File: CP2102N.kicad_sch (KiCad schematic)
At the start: 19 parts, among them J1 USB4110GFA, U9 CP2102N-A02-GQFN24R

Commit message: backups removalled schematic looking correct if not good
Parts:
- removed C15: 100nF, robot-cortex:C_0402_1005Metric, symbol robot-cortex:Capacitor
- removed D8: ESD9B3.3ST5G, robot-cortex:D_SOD-923, symbol robot-cortex:ESD9B3.3ST5G
- removed R4: 10k, robot-cortex:R_0402_1005Metric, symbol robot-cortex:Resistor
- added D4, D5: 150060GS84000, robot-cortex:LED_0603_1608Metric, symbol foc-pcb:LED
- added R2, R3: 470, robot-cortex:R_0402_1005Metric, symbol foc-pcb:Resistor
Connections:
- net 3V3: now also R2.1, R3.1; no longer C20.1, C21.1, U9.7 (VREGIN)
- net CP2102_RX: now also D4.1 (K)
- net CP2102_TX: now also D5.1 (K)
- net VUSB: now also C20.1, C21.1, U9.7 (VREGIN)
- net RS485: now reaches U9.12 (GPIO.2/RS485)
- net RTS: no longer names the net of U9.19 (~{RTS})
- new net: D4.2 (A), R2.2
- new net: D5.2 (A), R3.2
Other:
- note removed: "Tying VDD and VREGIN is for when the regulator is not used."
- moved on the sheet: C20, C21

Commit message: library table
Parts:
- C16, C17, C18, C19, C20, C21, C4: symbol robot-cortex:Capacitor -> usb-rs485:Capacitor
- D1, D2, D3: symbol robot-cortex:ESD9B3.3ST5G -> usb-rs485:ESD9B3.3ST5G
- D4, D5: symbol foc-pcb:LED -> usb-rs485:LED
- J1: symbol robot-cortex:USB4110GFA -> usb-rs485:USB4110GFA
- R1: symbol NeuralStimulatorAndRecorder:Resistor -> usb-rs485:Resistor
- R2, R3: symbol foc-pcb:Resistor -> usb-rs485:Resistor
- R7, R8, R9: symbol robot-cortex:Resistor -> usb-rs485:Resistor
- U9: symbol robot-cortex:CP2102N-A02-GQFN24R -> usb-rs485:CP2102N-A02-GQFN24R
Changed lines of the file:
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@@
     )
   )
-  (symbol (lib_id "robot-cortex:Resistor") (at 253.365 34.29 0) (mirror x) (unit 1)
+  (symbol (lib_id "usb-rs485:Resistor") (at 253.365 34.29 0) (mirror x) (unit 1)
     (in_bom yes) (on_board yes) (dnp no)
     (property "Reference" "R7" (at 250.825 33.655 0)
@@
     )
   )
-  (symbol (lib_id "robot-cortex:ESD9B3.3ST5G") (at 82.55 133.985 90) (unit 1)
+  (symbol (lib_id "usb-rs485:ESD9B3.3ST5G") (at 82.55 133.985 90) (unit 1)
     (in_bom yes) (on_board yes) (dnp no)
     (property "Reference" "D1" (at 78.74 133.985 90)
@@
     )
   )
-  (symbol (lib_id "robot-cortex:ESD9B3.3ST5G") (at 87.63 133.985 90) (unit 1)
+  (symbol (lib_id "usb-rs485:ESD9B3.3ST5G") (at 87.63 133.985 90) (unit 1)
     (in_bom yes) (on_board yes) (dnp no)
     (property "Reference" "D2" (at 85.09 133.985 90)
@@
     )
   )
-  (symbol (lib_id "robot-cortex:USB4110GFA") (at 112.395 108.585 0) (unit 1)
+  (symbol (lib_id "usb-rs485:USB4110GFA") (at 112.395 108.585 0) (unit 1)
     (in_bom yes) (on_board yes) (dnp no) (fields_autoplaced)
     (property "Reference" "J1" (at 112.395 93.345 0)
@@
     )
   )
-  (symbol (lib_id "robot-cortex:Capacitor") (at 186.69 102.87 0) (unit 1)
+  (symbol (lib_id "usb-rs485:Capacitor") (at 186.69 102.87 0) (unit 1)
     (in_bom yes) (on_board yes) (dnp no) (fields_autoplaced)
     (property "Reference" "C20" (at 189.865 102.235 0)
@@
     )
   )
-  (symbol (lib_id "robot-cortex:Capacitor") (at 198.12 102.87 0) (unit 1)
+  (symbol (lib_id "usb-rs485:Capacitor") (at 198.12 102.87 0) (unit 1)
     (in_bom yes) (on_board yes) (dnp no)
     (property "Reference" "C21" (at 200.66 102.235 0)
@@
     )
   )
-  (symbol (lib_id "robot-cortex:Capacitor") (at 57.15 36.195 0) (unit 1)
+  (symbol (lib_id "usb-rs485:Capacitor") (at 57.15 36.195 0) (unit 1)
     (in_bom yes) (on_board yes) (dnp no) (fields_autoplaced)
     (property "Reference" "C17" (at 60.325 35.56 0)
@@
     )
   )
-  (symbol (lib_id "robot-cortex:Capacitor") (at 69.85 36.83 0) (unit 1)
+  (symbol (lib_id "usb-rs485:Capacitor") (at 69.85 36.83 0) (unit 1)
     (in_bom yes) (on_board yes) (dnp no) (fields_autoplaced)
     (property "Reference" "C18" (at 73.025 36.195 0)
@@
     )
   )
-  (symbol (lib_id "foc-pcb:LED") (at 160.02 126.365 90) (unit 1)
+  (symbol (lib_id "usb-rs485:LED") (at 160.02 126.365 90) (unit 1)
     (in_bom yes) (on_board yes) (dnp no)
     (property "Reference" "D4" (at 155.575 126.365 90)
@@
     )
   )
-  (symbol (lib_id "robot-cortex:Resistor") (at 264.795 112.395 0) (mirror x) (unit 1)
+  (symbol (lib_id "usb-rs485:Resistor") (at 264.795 112.395 0) (mirror x) (unit 1)
     (in_bom yes) (on_board yes) (dnp no)
     (property "Reference" "R9" (at 262.89 109.855 90)
@@
     )
   )
-  (symbol (lib_id "robot-cortex:CP2102N-A02-GQFN24R") (at 234.315 128.905 0) (unit 1)
+  (symbol (lib_id "usb-rs485:CP2102N-A02-GQFN24R") (at 234.315 128.905 0) (unit 1)
     (in_bom yes) (on_board yes) (dnp no) (fields_autoplaced)
     (property "Reference" "U9" (at 234.315 100.965 0)
@@
     )
   )
-  (symbol (lib_id "robot-cortex:Capacitor") (at 44.45 36.195 0) (unit 1)
+  (symbol (lib_id "usb-rs485:Capacitor") (at 44.45 36.195 0) (unit 1)
     (in_bom yes) (on_board yes) (dnp no) (fields_autoplaced)
     (property "Reference" "C16" (at 47.625 35.56 0)
@@
     )
   )
-  (symbol (lib_id "foc-pcb:Resistor") (at 160.02 116.205 0) (unit 1)
+  (symbol (lib_id "usb-rs485:Resistor") (at 160.02 116.205 0) (unit 1)
     (in_bom yes) (on_board yes) (dnp no) (fields_autoplaced)
     (property "Reference" "R2" (at 162.56 116.84 0)
@@
     )
   )
-  (symbol (lib_id "robot-cortex:Resistor") (at 253.365 44.45 0) (mirror x) (unit 1)
+  (symbol (lib_id "usb-rs485:Resistor") (at 253.365 44.45 0) (mirror x) (unit 1)
     (in_bom yes) (on_board yes) (dnp no)
     (property "Reference" "R8" (at 250.4766 43.815 0)
@@
     )
   )
-  (symbol (lib_id "foc-pcb:Resistor") (at 166.37 116.205 0) (unit 1)
+  (symbol (lib_id "usb-rs485:Resistor") (at 166.37 116.205 0) (unit 1)
     (in_bom yes) (on_board yes) (dnp no) (fields_autoplaced)
     (property "Reference" "R3" (at 168.91 116.84 0)
@@
     )
   )
-  (symbol (lib_id "robot-cortex:Capacitor") (at 137.795 99.695 0) (unit 1)
+  (symbol (lib_id "usb-rs485:Capacitor") (at 137.795 99.695 0) (unit 1)
     (in_bom yes) (on_board yes) (dnp no) (fields_autoplaced)
     (property "Reference" "C4" (at 140.97 99.06 0)
@@
     )
   )
-  (symbol (lib_id "foc-pcb:LED") (at 166.37 126.365 90) (unit 1)
+  (symbol (lib_id "usb-rs485:LED") (at 166.37 126.365 90) (unit 1)
     (in_bom yes) (on_board yes) (dnp no)
     (property "Reference" "D5" (at 169.545 126.365 90)
@@
     )
   )
-  (symbol (lib_id "robot-cortex:ESD9B3.3ST5G") (at 92.71 133.985 90) (unit 1)
+  (symbol (lib_id "usb-rs485:ESD9B3.3ST5G") (at 92.71 133.985 90) (unit 1)
     (in_bom yes) (on_board yes) (dnp no)
     (property "Reference" "D3" (at 90.17 133.985 90)
@@
     )
   )
-  (symbol (lib_id "NeuralStimulatorAndRecorder:Resistor") (at 88.265 102.235 90) (unit 1)
+  (symbol (lib_id "usb-rs485:Resistor") (at 88.265 102.235 90) (unit 1)
     (in_bom yes) (on_board yes) (dnp no)
     (property "Reference" "R1" (at 90.805 99.695 90)
@@
     )
   )
-  (symbol (lib_id "robot-cortex:Capacitor") (at 81.28 36.83 0) (unit 1)
+  (symbol (lib_id "usb-rs485:Capacitor") (at 81.28 36.83 0) (unit 1)
     (in_bom yes) (on_board yes) (dnp no)
     (property "Reference" "C19" (at 83.82 36.195 0)

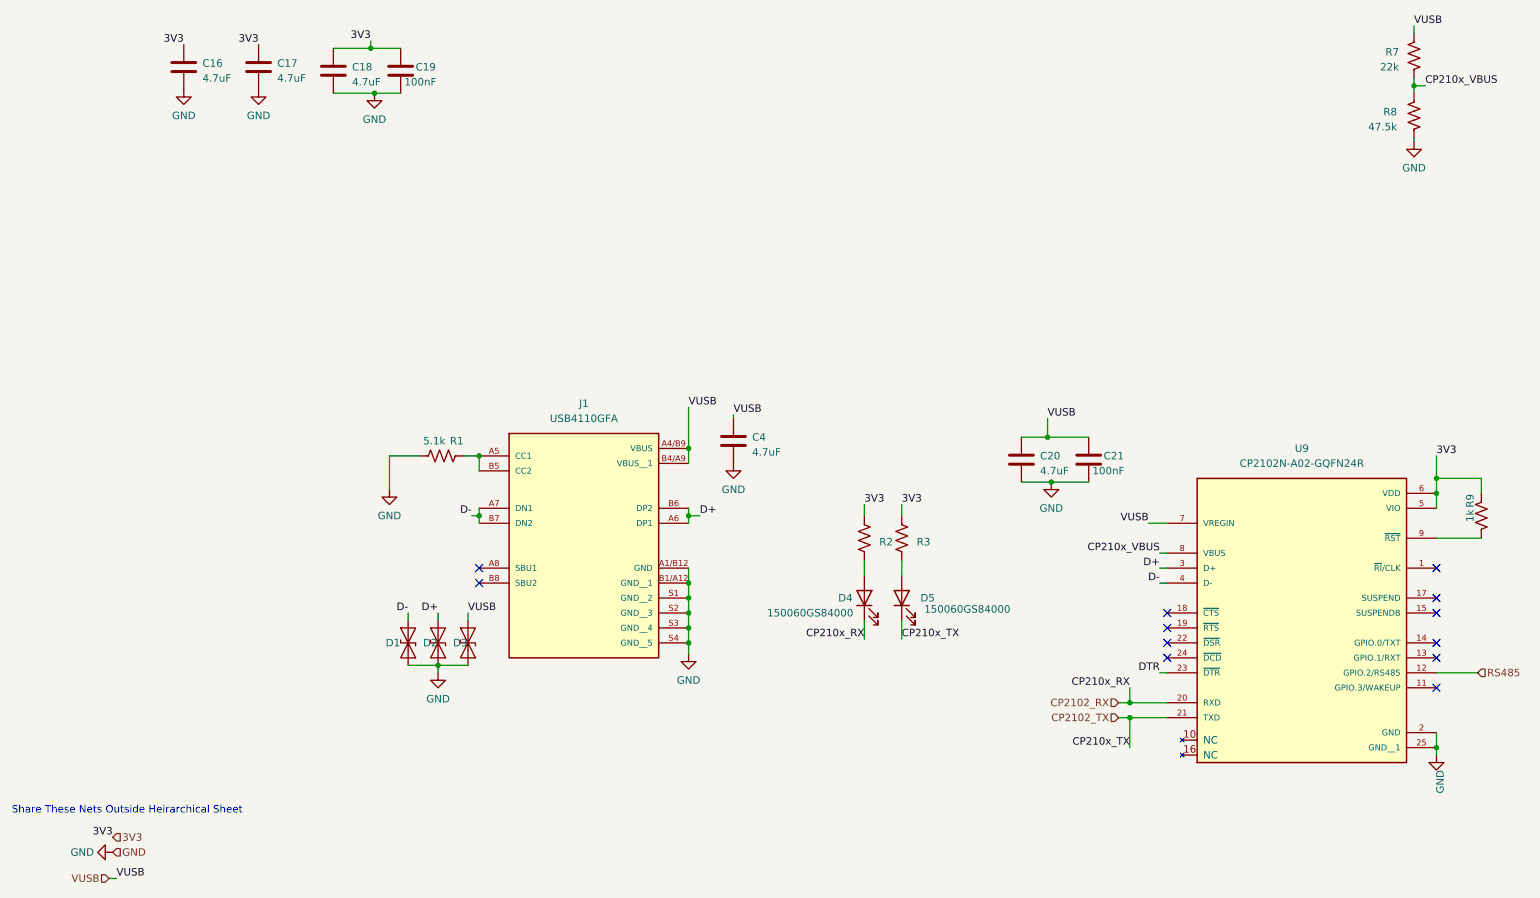
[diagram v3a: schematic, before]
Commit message: cleanup some routing
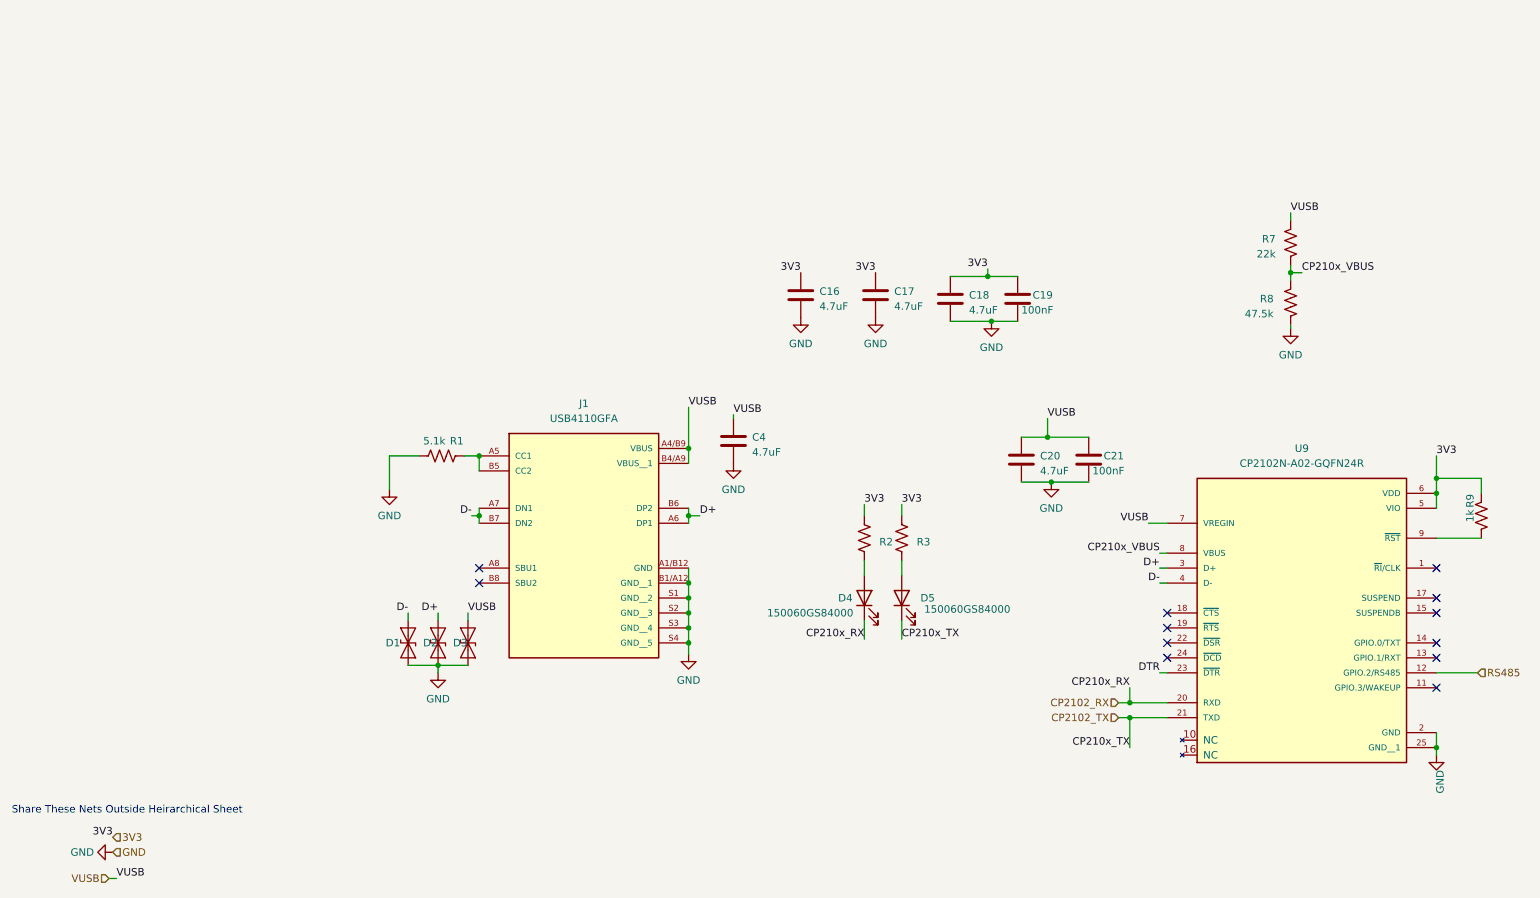
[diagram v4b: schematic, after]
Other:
- moved on the sheet: C16, C17, C18, C19, R7, R8

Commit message: routing
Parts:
- removed C16, C17, C18: 4.7uF, robot-cortex:C_0603_1608Metric, symbol usb-rs485:Capacitor
- removed C19: 100nF, robot-cortex:C_0402_1005Metric, symbol usb-rs485:Capacitor
- added C5: 4.7uF 0603, robot-cortex:C_0603_1608Metric, symbol usb-rs485:Capacitor
- added C8: 100nF, robot-cortex:C_0402_1005Metric, symbol usb-rs485:Capacitor
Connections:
- net GND: now also C5.2, C8.2
- new net +3V3: C5.1, C8.1

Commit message: rename library to be for this
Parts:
- C20, C4, C5: footprint robot-cortex:C_0603_1608Metric -> usb-rs485:C_0603_1608Metric
- C21, C8: footprint robot-cortex:C_0402_1005Metric -> usb-rs485:C_0402_1005Metric
- D1, D2, D3: footprint robot-cortex:D_SOD-923 -> usb-rs485:D_SOD-923
- D4, D5: footprint robot-cortex:LED_0603_1608Metric -> usb-rs485:LED_0603_1608Metric
- J1: footprint robot-cortex:GCT_USB4110GFA -> usb-rs485:GCT_USB4110GFA
- R1, R2, R3, R7, R8, R9: footprint robot-cortex:R_0402_1005Metric -> usb-rs485:R_0402_1005Metric
- U9: footprint robot-cortex:QFN50P400X400X80-25N -> usb-rs485:QFN50P400X400X80-25N
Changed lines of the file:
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@@
       (effects (font (size 1.27 1.27)) (justify right))
     )
-    (property "Footprint" "robot-cortex:R_0402_1005Metric" (at 227.33 78.74 0)
+    (property "Footprint" "usb-rs485:R_0402_1005Metric" (at 227.33 78.74 0)
       (effects (font (size 1.27 1.27)) hide)
     )
@@
       (effects (font (size 1.27 1.27)) (justify right) hide)
     )
-    (property "Footprint" "robot-cortex:D_SOD-923" (at 77.47 131.445 0)
+    (property "Footprint" "usb-rs485:D_SOD-923" (at 77.47 131.445 0)
       (effects (font (size 1.27 1.27)) hide)
     )
@@
       (effects (font (size 1.27 1.27)) (justify right) hide)
     )
-    (property "Footprint" "robot-cortex:D_SOD-923" (at 82.55 131.445 0)
+    (property "Footprint" "usb-rs485:D_SOD-923" (at 82.55 131.445 0)
       (effects (font (size 1.27 1.27)) hide)
     )
@@
       (effects (font (size 1.27 1.27)))
     )
-    (property "Footprint" "robot-cortex:GCT_USB4110GFA" (at 112.395 108.585 0)
+    (property "Footprint" "usb-rs485:GCT_USB4110GFA" (at 112.395 108.585 0)
       (effects (font (size 1.27 1.27)) (justify bottom) hide)
     )
@@
       (effects (font (size 1.27 1.27)) (justify left))
     )
-    (property "Footprint" "robot-cortex:C_0603_1608Metric" (at 187.6552 106.68 0)
+    (property "Footprint" "usb-rs485:C_0603_1608Metric" (at 187.6552 106.68 0)
       (effects (font (size 1.27 1.27)) hide)
     )
@@
       (effects (font (size 1.27 1.27)) (justify left))
     )
-    (property "Footprint" "robot-cortex:C_0402_1005Metric" (at 199.0852 106.68 0)
+    (property "Footprint" "usb-rs485:C_0402_1005Metric" (at 199.0852 106.68 0)
       (effects (font (size 1.27 1.27)) hide)
     )
@@
       (effects (font (size 1.27 1.27)) (justify left))
     )
-    (property "Footprint" "robot-cortex:C_0402_1005Metric" (at 115.9002 82.55 0)
+    (property "Footprint" "usb-rs485:C_0402_1005Metric" (at 115.9002 82.55 0)
       (effects (font (size 1.27 1.27)) hide)
     )
@@
       (effects (font (size 1.27 1.27)) (justify left))
     )
-    (property "Footprint" "robot-cortex:C_0603_1608Metric" (at 107.6198 82.55 0)
+    (property "Footprint" "usb-rs485:C_0603_1608Metric" (at 107.6198 82.55 0)
       (effects (font (size 1.27 1.27)) hide)
     )
@@
       (effects (font (size 1.27 1.27)) (justify right))
     )
-    (property "Footprint" "robot-cortex:LED_0603_1608Metric" (at 160.02 126.365 0)
+    (property "Footprint" "usb-rs485:LED_0603_1608Metric" (at 160.02 126.365 0)
       (effects (font (size 1.27 1.27)) hide)
     )
@@
       (effects (font (size 1.27 1.27)))
     )
-    (property "Footprint" "robot-cortex:R_0402_1005Metric" (at 259.715 125.095 0)
+    (property "Footprint" "usb-rs485:R_0402_1005Metric" (at 259.715 125.095 0)
       (effects (font (size 1.27 1.27)) hide)
     )
@@
       (effects (font (size 1.27 1.27)))
     )
-    (property "Footprint" "robot-cortex:QFN50P400X400X80-25N" (at 234.315 128.905 0)
+    (property "Footprint" "usb-rs485:QFN50P400X400X80-25N" (at 234.315 128.905 0)
       (effects (font (size 1.27 1.27)) (justify bottom) hide)
     )
@@
       (effects (font (size 1.27 1.27)) hide)
     )
-    (property "Footprint" "robot-cortex:R_0402_1005Metric" (at 154.94 103.505 0)
+    (property "Footprint" "usb-rs485:R_0402_1005Metric" (at 154.94 103.505 0)
       (effects (font (size 1.27 1.27)) hide)
     )
@@
       (effects (font (size 1.27 1.27)) (justify right))
     )
-    (property "Footprint" "robot-cortex:R_0402_1005Metric" (at 227.33 88.9 0)
+    (property "Footprint" "usb-rs485:R_0402_1005Metric" (at 227.33 88.9 0)
       (effects (font (size 1.27 1.27)) hide)
     )
@@
       (effects (font (size 1.27 1.27)) hide)
     )
-    (property "Footprint" "robot-cortex:R_0402_1005Metric" (at 161.29 103.505 0)
+    (property "Footprint" "usb-rs485:R_0402_1005Metric" (at 161.29 103.505 0)
       (effects (font (size 1.27 1.27)) hide)
     )
@@
       (effects (font (size 1.27 1.27)) (justify left))
     )
-    (property "Footprint" "robot-cortex:C_0603_1608Metric" (at 138.7602 103.505 0)
+    (property "Footprint" "usb-rs485:C_0603_1608Metric" (at 138.7602 103.505 0)
       (effects (font (size 1.27 1.27)) hide)
     )
@@
       (effects (font (size 1.27 1.27)) (justify right))
     )
-    (property "Footprint" "robot-cortex:LED_0603_1608Metric" (at 166.37 126.365 0)
+    (property "Footprint" "usb-rs485:LED_0603_1608Metric" (at 166.37 126.365 0)
       (effects (font (size 1.27 1.27)) hide)
     )
@@
       (effects (font (size 1.27 1.27)) (justify right) hide)
     )
-    (property "Footprint" "robot-cortex:D_SOD-923" (at 87.63 131.445 0)
+    (property "Footprint" "usb-rs485:D_SOD-923" (at 87.63 131.445 0)
       (effects (font (size 1.27 1.27)) hide)
     )
@@
       (effects (font (size 1.27 1.27)))
     )
-    (property "Footprint" "robot-cortex:R_0402_1005Metric" (at 75.565 107.315 0)
-      (effects (font (size 1.27 1.27)) hide)
-    )
+    (property "Footprint" "usb-rs485:R_0402_1005Metric" (at 75.565 107.315 0)
+      (effects (font (size 1.27 1.27)) hide)
+    )
